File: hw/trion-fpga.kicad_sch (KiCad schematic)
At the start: 0 parts

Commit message: WIP; converging
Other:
- sheet bank_1a_cfg ports: added CDON; removed CDONb
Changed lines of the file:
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@@
     (stroke (width 0) (type default))
   )
-  (hierarchical_label "CDONb" (shape output) (at 62.865 87.63 0) (fields_autoplaced)
+  (hierarchical_label "CDON" (shape output) (at 62.865 87.63 0) (fields_autoplaced)
     (effects (font (size 1.27 1.27)) (justify left))
   )
@@
       (effects (font (size 1.27 1.27)) (justify left top))
     )
-    (pin "CDONb" output (at 60.325 87.63 0)
+    (pin "CDON" output (at 60.325 87.63 0)
       (effects (font (size 1.27 1.27)) (justify right))
     )

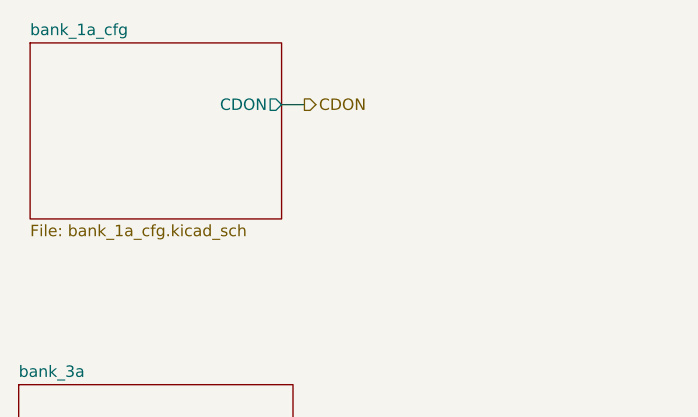
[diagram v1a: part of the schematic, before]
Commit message: added jumperable VDDIO for digital I/O, added reset generator
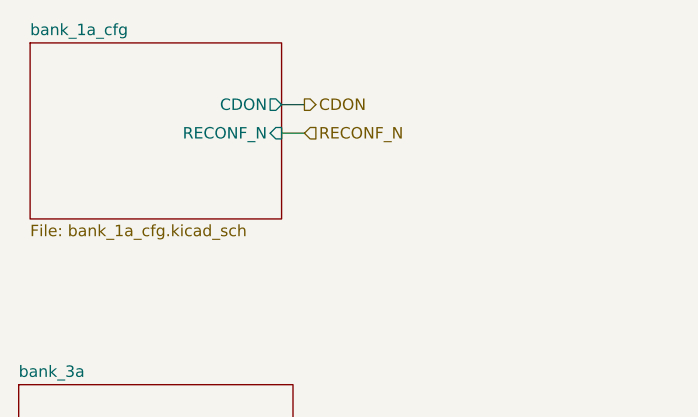
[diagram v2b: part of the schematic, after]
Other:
- sheet bank_1a_cfg ports: added RECONF_N; removed none
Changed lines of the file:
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@@
+    (stroke (width 0) (type default))
+  )
+  (wire (pts (xy 60.325 90.805) (xy 62.865 90.805))
     (stroke (width 0) (type default))
   )
   (hierarchical_label "CDON" (shape output) (at 62.865 87.63 0) (fields_autoplaced)
+    (effects (font (size 1.27 1.27)) (justify left))
+  )
+  (hierarchical_label "RECONF_N" (shape input) (at 62.865 90.805 0) (fields_autoplaced)
     (effects (font (size 1.27 1.27)) (justify left))
   )
@@
       (effects (font (size 1.27 1.27)) (justify right))
     )
+    (pin "RECONF_N" input (at 60.325 90.805 0)
+      (effects (font (size 1.27 1.27)) (justify right))
+    )

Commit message: connected versaclock CLKSEL to ULPI RSTB (share FPGA pin)
ULPI Rstb is unlikely to be used

Also: - update of kicad to 9.0 (many library footprints updated)
      - added sheet titles, author
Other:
- company: (none) -> Till Straumann
- title: (none) -> FPGA
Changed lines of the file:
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@@
 (kicad_sch
-	(version 20231120)
+	(version 20250114)
 	(generator "eeschema")
-	(generator_version "8.0")
+	(generator_version "9.0")
 	(paper "A4")
+	(title_block
+		(title "FPGA")
+		(rev "3.3b")
+		(company "Till Straumann")
+	)
 	(wire
 		(pts
@@
 		(at 31.75 161.29)
 		(size 30.48 24.13)
+		(exclude_from_sim no)
+		(in_bom yes)
+		(on_board yes)
+		(dnp no)
 		(fields_autoplaced yes)
 		(stroke
@@
 		(at 31.115 118.745)
 		(size 30.48 19.05)
+		(exclude_from_sim no)
+		(in_bom yes)
+		(on_board yes)
+		(dnp no)
 		(fields_autoplaced yes)
 		(stroke
@@
 		(at 92.075 161.925)
 		(size 30.48 26.67)
+		(exclude_from_sim no)
+		(in_bom yes)
+		(on_board yes)
+		(dnp no)
 		(fields_autoplaced yes)
 		(stroke
@@
 		(at 32.385 80.772)
 		(size 27.94 19.558)
+		(exclude_from_sim no)
+		(in_bom yes)
+		(on_board yes)
+		(dnp no)
 		(fields_autoplaced yes)
 		(stroke

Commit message: Added licensing information
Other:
- company: Till Straumann -> Copyright Till Straumann, 2025
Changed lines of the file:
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@@
 		(title "FPGA")
 		(rev "3.3b")
-		(company "Till Straumann")
+		(company "Copyright Till Straumann, 2025")
+		(comment 1 "License: CERN-OHL-P v2")
 	)
 	(wire
